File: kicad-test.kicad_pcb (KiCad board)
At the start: 2 copper layers, 7.6 x 13.6 mm, 2 parts

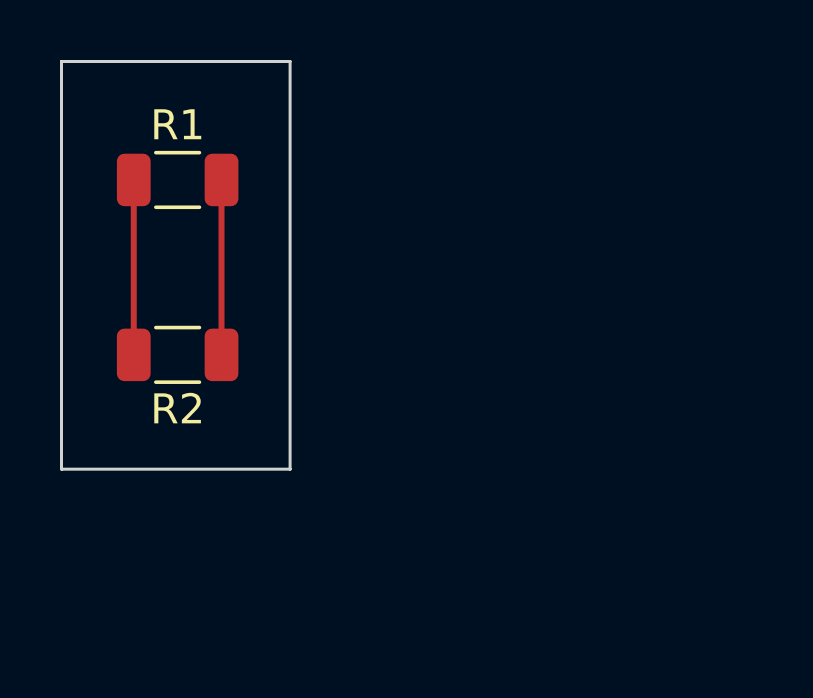
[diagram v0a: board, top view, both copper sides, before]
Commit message: added two extra resistors
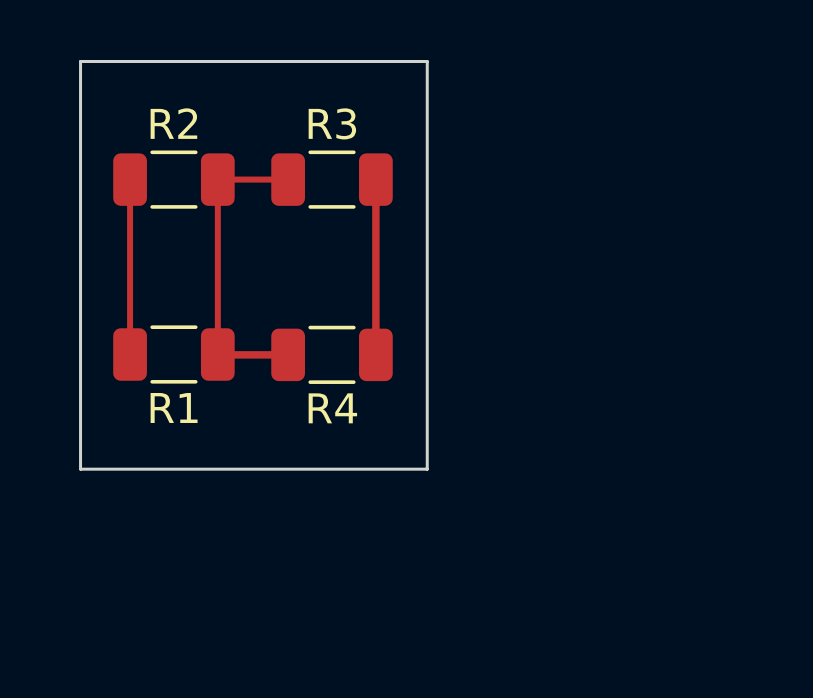
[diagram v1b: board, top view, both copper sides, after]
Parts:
- added R3: R, Resistor_SMD:R_1206_3216Metric, F.Cu at (111.6, 68.5)
- added R4: R, Resistor_SMD:R_1206_3216Metric, F.Cu at (111.6, 74.3)
- moved R2 5.84 mm to (106.4, 68.5), turned to 0 degrees
- moved R1 5.82 mm to (106.4, 74.3), turned to 180 degrees
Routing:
- net Net-(R3-Pad2): track 0.00 -> 5.84 mm
- net GND: track 5.83 -> 10.5 mm
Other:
- board size 7.6 x 13.6 mm -> 11.6 x 13.6 mm

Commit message: added button
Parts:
- added SW1: SW_Push, Button_Switch_THT:SW_PUSH_6mm_H8mm, F.Cu at (116.3, 69.2)
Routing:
- net GND: track 10.5 -> 45.5 mm
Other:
- board size 11.6 x 13.6 mm -> 22.4 x 13.6 mm
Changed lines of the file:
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@@
   (net 2 "Net-(R1-Pad2)")
   (net 3 "Net-(R3-Pad2)")
+  (footprint "Button_Switch_THT:SW_PUSH_6mm_H8mm" (layer "F.Cu")
+    (at 116.309 69.16)
+    (descr "tactile push button, 6x6mm e.g. PHAP33xx series, height=8mm")
+    (tags "tact sw push 6mm")
+    (property "Sheetfile" "kicad-test.kicad_sch")
+    (property "Sheetname" "")
+    (property "ki_description" "Push button switch, generic, two pins")
+    (property "ki_keywords" "switch normally-open pushbutton push-button")
+    (attr through_hole)
+    (fp_text reference "SW1" (at 3.25 -2) (layer "F.SilkS")
+        (effects (font (size 1 1) (thickness 0.15)))
+    )
+    (fp_text value "SW_Push" (at 3.75 6.7) (layer "F.Fab")
+        (effects (font (size 1 1) (thickness 0.15)))
+    )
+    (fp_text user "${REFERENCE}" (at 3.25 2.25) (layer "F.Fab")
+        (effects (font (size 1 1) (thickness 0.15)))
+    )
+    (fp_line (start -0.25 1.5) (end -0.25 3)
+      (stroke (width 0.12) (type solid)) (layer "F.SilkS"))
+    (fp_line (start 1 5.5) (end 5.5 5.5)
+      (stroke (width 0.12) (type solid)) (layer "F.SilkS"))
+    (fp_line (start 5.5 -1) (end 1 -1)
+      (stroke (width 0.12) (type solid)) (layer "F.SilkS"))
+    (fp_line (start 6.75 3) (end 6.75 1.5)
+      (stroke (width 0.12) (type solid)) (layer "F.SilkS"))
+    (fp_line (start -1.5 -1.5) (end -1.25 -1.5)
+      (stroke (width 0.05) (type solid)) (layer "F.CrtYd"))
+    (fp_line (start -1.5 -1.25) (end -1.5 -1.5)
+      (stroke (width 0.05) (type solid)) (layer "F.CrtYd"))
+    (fp_line (start -1.5 5.75) (end -1.5 -1.25)
+      (stroke (width 0.05) (type solid)) (layer "F.CrtYd"))
+    (fp_line (start -1.5 5.75) (end -1.5 6)
+      (stroke (width 0.05) (type solid)) (layer "F.CrtYd"))
+    (fp_line (start -1.5 6) (end -1.25 6)
+      (stroke (width 0.05) (type solid)) (layer "F.CrtYd"))
+    (fp_line (start -1.25 -1.5) (end 7.75 -1.5)
+      (stroke (width 0.05) (type solid)) (layer "F.CrtYd"))
+    (fp_line (start 7.75 -1.5) (end 8 -1.5)
+      (stroke (width 0.05) (type solid)) (layer "F.CrtYd"))
+    (fp_line (start 7.75 6) (end -1.25 6)
+      (stroke (width 0.05) (type solid)) (layer "F.CrtYd"))
+    (fp_line (start 7.75 6) (end 8 6)
+      (stroke (width 0.05) (type solid)) (layer "F.CrtYd"))
+    (fp_line (start 8 -1.5) (end 8 -1.25)
+      (stroke (width 0.05) (type solid)) (layer "F.CrtYd"))
+    (fp_line (start 8 -1.25) (end 8 5.75)
+      (stroke (width 0.05) (type solid)) (layer "F.CrtYd"))
+    (fp_line (start 8 6) (end 8 5.75)
+      (stroke (width 0.05) (type solid)) (layer "F.CrtYd"))
+    (fp_line (start 0.25 -0.75) (end 3.25 -0.75)
+      (stroke (width 0.1) (type solid)) (layer "F.Fab"))
+    (fp_line (start 0.25 5.25) (end 0.25 -0.75)
+      (stroke (width 0.1) (type solid)) (layer "F.Fab"))
+    (fp_line (start 3.25 -0.75) (end 6.25 -0.75)
+      (stroke (width 0.1) (type solid)) (layer "F.Fab"))
+    (fp_line (start 6.25 -0.75) (end 6.25 5.25)
+      (stroke (width 0.1) (type solid)) (layer "F.Fab"))
+    (fp_line (start 6.25 5.25) (end 0.25 5.25)
+      (stroke (width 0.1) (type solid)) (layer "F.Fab"))
+    (fp_circle (center 3.25 2.25) (end 1.25 2.5)
+      (stroke (width 0.1) (type solid)) (fill none) (layer "F.Fab"))
+    (pad "1" thru_hole circle (at 0 0 90) (size 2 2) (drill 1.1) (layers "*.Cu" "*.Mask")
+      (net 1 "GND") (pinfunction "1") (pintype "passive"))
+    (pad "1" thru_hole circle (at 6.5 0 90) (size 2 2) (drill 1.1) (layers "*.Cu" "*.Mask")
+      (net 1 "GND") (pinfunction "1") (pintype "passive"))
+    (pad "2" thru_hole circle (at 0 4.5 90) (size 2 2) (drill 1.1) (layers "*.Cu" "*.Mask")
+      (net 1 "GND") (pinfunction "2") (pintype "passive"))
+    (pad "2" thru_hole circle (at 6.5 4.5 90) (size 2 2) (drill 1.1) (layers "*.Cu" "*.Mask")
+      (net 1 "GND") (pinfunction "2") (pintype "passive"))
+    (model "${KICAD6_3DMODEL_DIR}/Button_Switch_THT.3dshapes/SW_PUSH_6mm_H8mm.wrl"
+      (offset (xyz 0 0 0))
+      (scale (xyz 1 1 1))
+      (rotate (xyz 0 0 0))
+    )
+  )
   (footprint "Resistor_SMD:R_1206_3216Metric" (layer "F.Cu")
     (at 111.633 68.453)
@@
     )
   )
-  (gr_rect (start 103.251 64.516) (end 114.808 78.105)
+  (gr_rect (start 103.251 64.516) (end 125.603 78.105)
     (stroke (width 0.1) (type default)) (fill none) (layer "Edge.Cuts"))
+  (segment (start 107.827 74.283) (end 107.827 76.196) (width 0.2) (layer "F.Cu") (net 1))
+  (segment (start 116.309 69.16) (end 122.809 69.16) (width 0.25) (layer "F.Cu") (net 1))
+  (segment (start 107.823 76.2) (end 116.309 76.2) (width 0.2) (layer "F.Cu") (net 1))
+  (segment (start 122.809 69.16) (end 122.809 73.66) (width 0.25) (layer "F.Cu") (net 1))
   (segment (start 107.827 74.283) (end 107.827 68.453) (width 0.2) (layer "F.Cu") (net 1))
   (segment (start 107.839 74.295) (end 107.827 74.283) (width 0.25) (layer "F.Cu") (net 1))
+  (segment (start 116.309 76.2) (end 116.309 69.16) (width 0.2) (layer "F.Cu") (net 1))
+  (segment (start 107.827 76.196) (end 107.823 76.2) (width 0.2) (layer "F.Cu") (net 1))
   (segment (start 107.827 68.453) (end 110.1705 68.453) (width 0.2) (layer "F.Cu") (net 1))
   (segment (start 110.1705 74.295) (end 107.839 74.295) (width 0.25) (layer "F.Cu") (net 1))
+  (segment (start 122.809 73.66) (end 116.309 73.66) (width 0.25) (layer "F.Cu") (net 1))
   (segment (start 104.902 68.453) (end 104.902 74.283) (width 0.2) (layer "F.Cu") (net 2))
   (segment (start 113.0955 68.453) (end 113.0955 74.295) (width 0.25) (layer "F.Cu") (net 3))

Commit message: added two leds
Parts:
- added D1: LED, LED_SMD:LED_1210_3225Metric, F.Cu at (114.1, 79.2)
- added D2: LED, LED_SMD:LED_1210_3225Metric, F.Cu at (109.9, 79.2)
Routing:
- net GND: track 45.5 -> 53.4 mm
- net Net-(D1-A): track 0.00 -> 4.29 mm
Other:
- board size 22.4 x 13.6 mm -> 22.4 x 19.2 mm
- board text added: "Text Test"
- board text added: "V1.0"
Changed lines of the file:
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@@
   (net 2 "Net-(R1-Pad2)")
   (net 3 "Net-(R3-Pad2)")
+  (net 4 "Net-(D1-A)")
   (footprint "Button_Switch_THT:SW_PUSH_6mm_H8mm" (layer "F.Cu")
     (at 116.309 69.16)
@@
     )
   )
+  (footprint "LED_SMD:LED_1210_3225Metric" (layer "F.Cu")
+    (at 114.145 79.245 -90)
+    (descr "LED SMD 1210 (3225 Metric), square (rectangular) end terminal, IPC_7351 nominal, (Body size source: http://www.tortai-tech.com/upload/download/2011102023233369053.pdf), generated with kicad-footprint-generator")
+    (tags "LED")
+    (property "Sheetfile" "kicad-test.kicad_sch")
+    (property "Sheetname" "")
+    (property "ki_description" "Light emitting diode")
+    (property "ki_keywords" "LED diode")
+    (attr smd)
+    (fp_text reference "D1" (at 3.051 -0.028 -180) (layer "F.SilkS")
+        (effects (font (size 1 1) (thickness 0.15)))
+    )
+    (fp_text value "LED" (at 0 2.28 90) (layer "F.Fab")
+        (effects (font (size 1 1) (thickness 0.15)))
+    )
+    (fp_text user "${REFERENCE}" (at 0 0 90) (layer "F.Fab")
+        (effects (font (size 0.8 0.8) (thickness 0.12)))
+    )
+    (fp_line (start -2.285 -1.585) (end -2.285 1.585)
+      (stroke (width 0.12) (type solid)) (layer "F.SilkS"))
+    (fp_line (start -2.285 1.585) (end 1.6 1.585)
+      (stroke (width 0.12) (type solid)) (layer "F.SilkS"))
+    (fp_line (start 1.6 -1.585) (end -2.285 -1.585)
+      (stroke (width 0.12) (type solid)) (layer "F.SilkS"))
+    (fp_line (start -2.28 -1.58) (end 2.28 -1.58)
+      (stroke (width 0.05) (type solid)) (layer "F.CrtYd"))
+    (fp_line (start -2.28 1.58) (end -2.28 -1.58)
+      (stroke (width 0.05) (type solid)) (layer "F.CrtYd"))
+    (fp_line (start 2.28 -1.58) (end 2.28 1.58)
+      (stroke (width 0.05) (type solid)) (layer "F.CrtYd"))
+    (fp_line (start 2.28 1.58) (end -2.28 1.58)
+      (stroke (width 0.05) (type solid)) (layer "F.CrtYd"))
+    (fp_line (start -1.6 -0.625) (end -1.6 1.25)
+      (stroke (width 0.1) (type solid)) (layer "F.Fab"))
+    (fp_line (start -1.6 1.25) (end 1.6 1.25)
+      (stroke (width 0.1) (type solid)) (layer "F.Fab"))
+    (fp_line (start -0.975 -1.25) (end -1.6 -0.625)
+      (stroke (width 0.1) (type solid)) (layer "F.Fab"))
+    (fp_line (start 1.6 -1.25) (end -0.975 -1.25)
+      (stroke (width 0.1) (type solid)) (layer "F.Fab"))
+    (fp_line (start 1.6 1.25) (end 1.6 -1.25)
+      (stroke (width 0.1) (type solid)) (layer "F.Fab"))
+    (pad "1" smd roundrect (at -1.4 0 270) (size 1.25 2.65) (layers "F.Cu" "F.Paste" "F.Mask") (roundrect_rratio 0.2)
+      (net 1 "GND") (pinfunction "K") (pintype "passive"))
+    (pad "2" smd roundrect (at 1.4 0 270) (size 1.25 2.65) (layers "F.Cu" "F.Paste" "F.Mask") (roundrect_rratio 0.2)
+      (net 4 "Net-(D1-A)") (pinfunction "A") (pintype "passive"))
+    (model "${KICAD6_3DMODEL_DIR}/LED_SMD.3dshapes/LED_1210_3225Metric.wrl"
+      (offset (xyz 0 0 0))
+      (scale (xyz 1 1 1))
+      (rotate (xyz 0 0 0))
+    )
+  )
   (footprint "Resistor_SMD:R_1206_3216Metric" (layer "F.Cu")
     (at 106.3645 74.283 180)
@@
     )
   )
+  (footprint "LED_SMD:LED_1210_3225Metric" (layer "F.Cu")
+    (at 109.855 79.245 -90)
+    (descr "LED SMD 1210 (3225 Metric), square (rectangular) end terminal, IPC_7351 nominal, (Body size source: http://www.tortai-tech.com/upload/download/2011102023233369053.pdf), generated with kicad-footprint-generator")
+    (tags "LED")
+    (property "Sheetfile" "kicad-test.kicad_sch")
+    (property "Sheetname" "")
+    (property "ki_description" "Light emitting diode")
+    (property "ki_keywords" "LED diode")
+    (attr smd)
+    (fp_text reference "D2" (at 3.051 0 -180) (layer "F.SilkS")
+        (effects (font (size 1 1) (thickness 0.15)))
+    )
+    (fp_text value "LED" (at 0 2.28 90) (layer "F.Fab")
+        (effects (font (size 1 1) (thickness 0.15)))
+    )
+    (fp_text user "${REFERENCE}" (at 0 0 90) (layer "F.Fab")
+        (effects (font (size 0.8 0.8) (thickness 0.12)))
+    )
+    (fp_line (start -2.285 -1.585) (end -2.285 1.585)
+      (stroke (width 0.12) (type solid)) (layer "F.SilkS"))
+    (fp_line (start -2.285 1.585) (end 1.6 1.585)
+      (stroke (width 0.12) (type solid)) (layer "F.SilkS"))
+    (fp_line (start 1.6 -1.585) (end -2.285 -1.585)
+      (stroke (width 0.12) (type solid)) (layer "F.SilkS"))
+    (fp_line (start -2.28 -1.58) (end 2.28 -1.58)
+      (stroke (width 0.05) (type solid)) (layer "F.CrtYd"))
+    (fp_line (start -2.28 1.58) (end -2.28 -1.58)
+      (stroke (width 0.05) (type solid)) (layer "F.CrtYd"))
+    (fp_line (start 2.28 -1.58) (end 2.28 1.58)
+      (stroke (width 0.05) (type solid)) (layer "F.CrtYd"))
+    (fp_line (start 2.28 1.58) (end -2.28 1.58)
+      (stroke (width 0.05) (type solid)) (layer "F.CrtYd"))
+    (fp_line (start -1.6 -0.625) (end -1.6 1.25)
+      (stroke (width 0.1) (type solid)) (layer "F.Fab"))
+    (fp_line (start -1.6 1.25) (end 1.6 1.25)
+      (stroke (width 0.1) (type solid)) (layer "F.Fab"))
+    (fp_line (start -0.975 -1.25) (end -1.6 -0.625)
+      (stroke (width 0.1) (type solid)) (layer "F.Fab"))
+    (fp_line (start 1.6 -1.25) (end -0.975 -1.25)
+      (stroke (width 0.1) (type solid)) (layer "F.Fab"))
+    (fp_line (start 1.6 1.25) (end 1.6 -1.25)
+      (stroke (width 0.1) (type solid)) (layer "F.Fab"))
+    (pad "1" smd roundrect (at -1.4 0 270) (size 1.25 2.65) (layers "F.Cu" "F.Paste" "F.Mask") (roundrect_rratio 0.2)
+      (net 1 "GND") (pinfunction "K") (pintype "passive"))
+    (pad "2" smd roundrect (at 1.4 0 270) (size 1.25 2.65) (layers "F.Cu" "F.Paste" "F.Mask") (roundrect_rratio 0.2)
+      (net 4 "Net-(D1-A)") (pinfunction "A") (pintype "passive"))
+    (model "${KICAD6_3DMODEL_DIR}/LED_SMD.3dshapes/LED_1210_3225Metric.wrl"
+      (offset (xyz 0 0 0))
+      (scale (xyz 1 1 1))
+      (rotate (xyz 0 0 0))
+    )
+  )
   (footprint "Resistor_SMD:R_1206_3216Metric" (layer "F.Cu")
     (at 111.633 74.295 180)
@@
     )
   )
-  (gr_rect (start 103.251 64.516) (end 125.603 78.105)
+  (gr_rect (start 103.251 64.516) (end 125.603 83.693)
     (stroke (width 0.1) (type default)) (fill none) (layer "Edge.Cuts"))
+  (gr_text "Text Test" (at 117.094 79.248) (layer "F.SilkS")
+    (effects (font (size 1 1) (thickness 0.15)) (justify left bottom))
+  )
+  (gr_text "V1.0" (at 117.348 80.899) (layer "F.SilkS")
+    (effects (font (size 1 1) (thickness 0.15)) (justify left bottom))
+  )
   (segment (start 107.827 74.283) (end 107.827 76.196) (width 0.2) (layer "F.Cu") (net 1))
   (segment (start 116.309 69.16) (end 122.809 69.16) (width 0.25) (layer "F.Cu") (net 1))
@@
   (segment (start 107.827 68.453) (end 110.1705 68.453) (width 0.2) (layer "F.Cu") (net 1))
   (segment (start 110.1705 74.295) (end 107.839 74.295) (width 0.25) (layer "F.Cu") (net 1))
+  (segment (start 110.1705 74.295) (end 110.1705 77.5295) (width 0.25) (layer "F.Cu") (net 1))
+  (segment (start 110.1705 77.5295) (end 109.855 77.845) (width 0.25) (layer "F.Cu") (net 1))
   (segment (start 122.809 73.66) (end 116.309 73.66) (width 0.25) (layer "F.Cu") (net 1))
+  (segment (start 109.855 77.845) (end 114.145 77.845) (width 0.25) (layer "F.Cu") (net 1))
   (segment (start 104.902 68.453) (end 104.902 74.283) (width 0.2) (layer "F.Cu") (net 2))
   (segment (start 113.0955 68.453) (end 113.0955 74.295) (width 0.25) (layer "F.Cu") (net 3))
+  (segment (start 109.855 80.645) (end 114.145 80.645) (width 0.25) (layer "F.Cu") (net 4))
 )
